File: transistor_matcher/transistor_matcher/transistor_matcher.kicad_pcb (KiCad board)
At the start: 2 copper layers, 41.9 x 40 mm, 21 parts, among them J1 USB_B_Micro, J2 ISP, J3 14x4 Segment Display (I2C), Q1 2N3904, Q2 BJT, SW1 MODE, SW2 REVERSE, U1 AD8223, U2 ATtiny85

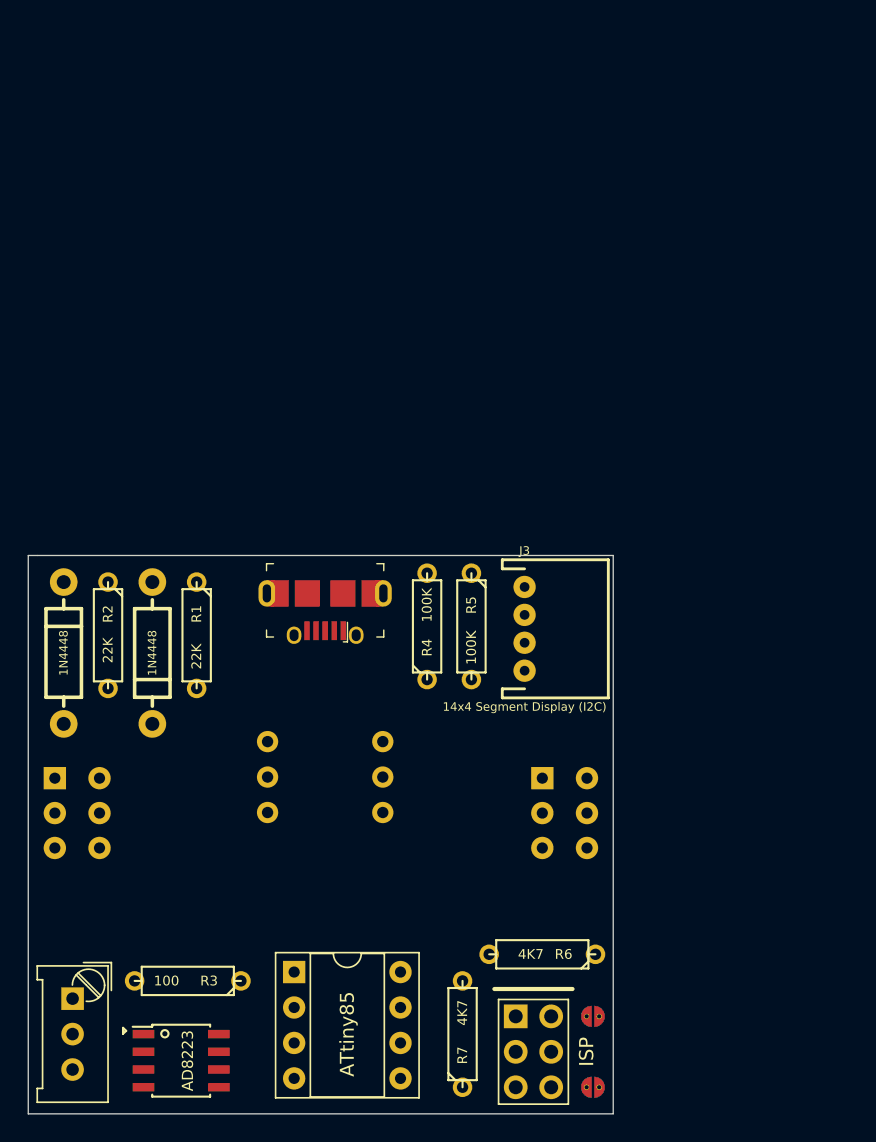
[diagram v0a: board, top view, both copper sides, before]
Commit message: simplfied based on emperical tests
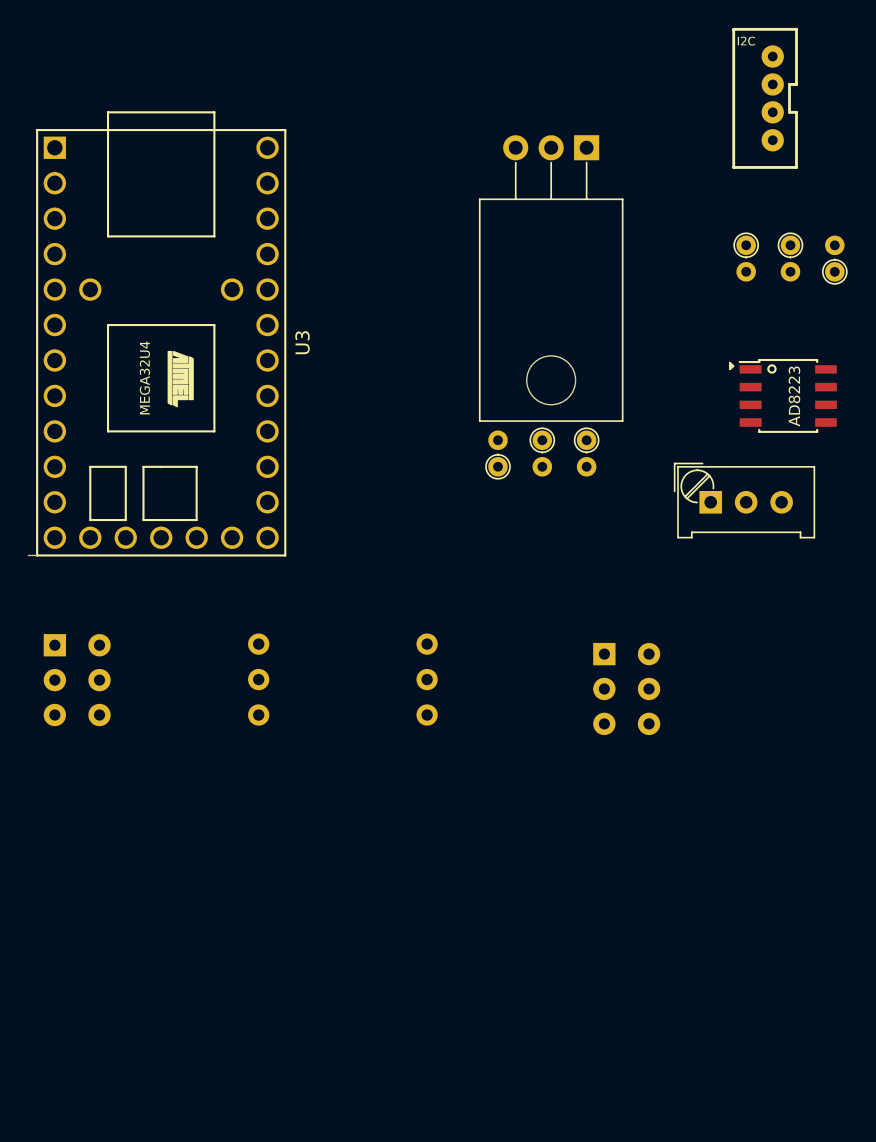
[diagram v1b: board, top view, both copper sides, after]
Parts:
- removed D1, D2: 1N4448, sparkfun/SparkFun-KiCad-Libraries/Footprints/Silicon-Custom.pretty:DIODE-1N4001
- removed J1: USB_B_Micro, digikey/digikey-kicad-library/digikey-footprints.pretty:USB_Micro_AB_Female_0475890001
- removed J2: ISP, 4ms/4ms-kicad-lib/lib-footprints/4ms_Connector.pretty:Pins_2x03_2.54mm_TH_ISP
- removed JP1, JP2: Jumper, keebio/Keebio-Parts.pretty:solder_jumper
- removed R2: 22K, 4ms/4ms-kicad-lib/4ms-footprints.pretty:Resistor_TH_300
- added U3: Teensy2.0_(Arduino), teensy:Teensy2.0, F.Cu at (93.3, 41.9)
- J3: value 14x4 Segment Display (I2C) -> I2C; footprint sparkfun/SparkFun-KiCad-Libraries/Footprints/Connectors.pretty:JST-4-PTH -> sparkfun/SparkFun-KiCad-Libraries/Footprints/Connectors.pretty:JST-4-PTH-VERT
- Q2: value BJT -> 2N3904
- R1: value 22K -> 10K; footprint 4ms/4ms-kicad-lib/4ms-footprints.pretty:Resistor_TH_300 -> KiCad/Resistors_ThroughHole.pretty:R_Axial_DIN0204_L3.6mm_D1.6mm_P1.90mm_Vertical
- R3, R6, R7: footprint 4ms/4ms-kicad-lib/4ms-footprints.pretty:Resistor_TH_300 -> KiCad/Resistors_ThroughHole.pretty:R_Axial_DIN0204_L3.6mm_D1.6mm_P1.90mm_Vertical
- R4, R5: value 100K -> 220; footprint 4ms/4ms-kicad-lib/4ms-footprints.pretty:Resistor_TH_300 -> KiCad/Resistors_ThroughHole.pretty:R_Axial_DIN0204_L3.6mm_D1.6mm_P1.90mm_Vertical
- RV1: value 10K TRIM -> 50K TRIM
- SW1: value MODE -> SW_DPDT_x2
- SW2: value REVERSE -> SW_DPDT_x2
- U2: value ATtiny85 -> LM317_3PinPackage; footprint KiCad/Housings_DIP.pretty:DIP-8_W7.62mm_Socket -> KiCad/TO_SOT_Packages_THT.pretty:TO-220-3_Horizontal
- moved R3 68.8 mm to (141.6, 36.8), turned to 90 degrees
- moved U1 64.5 mm to (138.3, 45.7)
- moved U2 62.7 mm to (123.8, 27.9), turned to 180 degrees
- moved R7 60.1 mm to (135.3, 34.9), turned to 270 degrees
- moved RV1 57.9 mm to (132.7, 53.3), turned to 0 degrees
- moved R6 53.8 mm to (138.4, 34.9), turned to 270 degrees
- moved J3 41.7 mm to (136.6, 24.4), turned to 90 degrees
- moved R1 31.2 mm to (123.8, 48.9)
- moved R4 15.7 mm to (120.7, 48.9), turned to 270 degrees
- moved R5 11.6 mm to (117.5, 50.8), turned to 90 degrees
- moved SW1 9.94 mm to (125.1, 64.2)
- moved SW2 9.53 mm to (85.7, 63.6)
- moved Q2 7.67 mm to (112.4, 66.0)
- moved Q1 7.01 mm to (100.3, 66.0)
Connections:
- net Net-(J3-Pad3) renamed SDA
- net Net-(J3-Pad4) renamed SCL
- J3 pad 2: VCC -> +5V
- R1 pad 1: Net-(D1-PadA) -> Net-(Q1-Pad3)
- R1 pad 2: VCC -> Net-(R1-Pad2)
- R4 pad 1: VREF -> Net-(R4-Pad1)
- R4 pad 2: VCC -> VREF
- R5 pad 2: VREF -> Net-(R4-Pad1)
- R6 pad 2: VCC -> +5V
- R7 pad 2: VCC -> +5V
- SW1 pad 1: Net-(D1-PadA) -> +5V
- SW1 pad 2: Net-(Q1-Pad3) -> Net-(R1-Pad2)
- SW1 pad 3: Net-(D2-PadC) -> GND
- SW1 pad 6: VCC -> +5V
- U1 pad 7: VCC -> +5V
- U2 pad 1: RST -> Net-(R4-Pad1)
- U2 pad 2: Net-(U2-Pad2) -> VREF
- U2 pad 3: AOUT -> +5V
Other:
- board outline removed
